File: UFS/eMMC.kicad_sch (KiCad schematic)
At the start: 7 parts, among them J13 513383474

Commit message: Relink hierarchical root: 18 sheets into RK3576 SBCv2 top level
Root was empty (no sheet boxes); all subsheets orphaned.
Rebuilt A1 top level linking RK3576, LPDDR5, Power, Ethernet,
HDMI, MIPI, PCIe, USB-A/C, Wireless, RTC, uSD, GPIO, OLED,
RP2350A, Connectors, Fixtures, DC_Power. block_diagrame kept
docs-only (unlinked, avoids double-instantiation). Lowercase
stub duplicates excluded. ERC: 1388 -> 770 violations.
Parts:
- renumbered C149 to C334, C147 to C335, C150 to C336, C148 to C337, C144 to C338, C143 to C339, J13 to J20
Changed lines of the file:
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@@
 		(polyline
 			(pts
-				(xy 57.785 33.02) (xy 43.815 33.02) (xy 43.815 50.165) (xy 57.785 50.165)
+				(xy 60.96 87.9475) (xy 60.96 65.405) (xy 40.64 65.4049) (xy 40.64 87.9474)
 			)
 			(stroke
 				(width 0)
 				(type dash)
-				(color 89 32 227 1)
+				(color 255 0 26 1)
 			)
 			(fill
@@
 		(polyline
 			(pts
-				(xy 60.96 64.77) (xy 42.545 64.77) (xy 42.545 88.9) (xy 60.96 88.9)
+				(xy 57.785 33.02) (xy 43.815 33.02) (xy 43.815 50.165) (xy 57.785 50.165)
 			)
 			(stroke
@@
 		(polyline
 			(pts
-				(xy 104.775 34.29) (xy 118.745 34.29) (xy 118.745 51.435) (xy 104.775 51.435)
+				(xy 61.595 64.77) (xy 42.545 64.77) (xy 42.545 88.9) (xy 61.595 88.9)
 			)
 			(stroke
@@
 			(fill
 				(type none)
+			)
+		)
+	)
+	(rule_area
+		(exclude_from_sim no)
+		(in_bom yes)
+		(on_board yes)
+		(dnp no)
+		(polyline
+			(pts
+				(xy 105.41 49.53) (xy 105.41 34.925) (xy 120.65 34.9249) (xy 120.65 49.5299)
+			)
+			(stroke
+				(width 0)
+				(type dash)
+				(color 255 0 26 1)
+			)
+			(fill
+				(type none)
+			)
+		)
+	)
+	(rule_area
+		(exclude_from_sim no)
+		(in_bom yes)
+		(on_board yes)
+		(dnp no)
+		(polyline
+			(pts
+				(xy 104.775 34.29) (xy 118.11 34.29) (xy 118.11 50.165) (xy 104.775 50.165)
+			)
+			(stroke
+				(width 0)
+				(type dash)
+				(color 89 32 227 1)
+			)
+			(fill
+				(type none)
+			)
+		)
+	)
+	(rule_area
+		(exclude_from_sim no)
+		(in_bom yes)
+		(on_board yes)
+		(dnp no)
+		(polyline
+			(pts
+				(xy 57.15 48.26) (xy 57.15 33.655) (xy 41.91 33.6549) (xy 41.91 48.2599)
+			)
+			(stroke
+				(width 0)
+				(type dash)
+				(color 255 0 26 1)
+			)
+			(fill
+				(type none)
+			)
+		)
+	)
+	(netclass_flag "Under PGA"
+		(length 1.27)
+		(shape round)
+		(at 120.65 35.56 270)
+		(effects
+			(font
+				(size 1.27 1.27)
+			)
+			(justify right bottom)
+		)
+		(property "Netclass" "100 OHM"
+			(at 125.476 35.56 0)
+			(show_name no)
+			(do_not_autoplace no)
+			(effects
+				(font
+					(size 0.762 0.762)
+					(color 255 0 26 1)
+				)
 			)
 		)
@@
 	)
 	(netclass_flag "Under PGA"
+		(length 1.27)
+		(shape round)
+		(at 41.91 34.29 90)
+		(effects
+			(font
+				(size 1.27 1.27)
+			)
+			(justify left bottom)
+		)
+		(property "Netclass" "100 OHM"
+			(at 37.084 34.29 0)
+			(show_name no)
+			(do_not_autoplace no)
+			(effects
+				(font
+					(size 0.762 0.762)
+					(color 255 0 26 1)
+				)
+			)
+		)
+	)
+	(netclass_flag "Under PGA"
 		(length 2.54)
 		(shape round)
@@
 				(font
 					(size 1.27 1.27)
+				)
+			)
+		)
+	)
+	(netclass_flag "Under PGA"
+		(length 1.27)
+		(shape round)
+		(at 40.64 66.04 90)
+		(effects
+			(font
+				(size 1.27 1.27)
+			)
+			(justify left bottom)
+		)
+		(property "Netclass" "50 OHM"
+			(at 36.068 66.04 0)
+			(show_name no)
+			(do_not_autoplace no)
+			(effects
+				(font
+					(size 0.762 0.762)
+					(color 255 0 26 1)
 				)
 			)
@@
 		(dnp no)
 		(fields_autoplaced yes)
-		(property "Reference" "J13"
+		(property "Reference" "J20"
 			(at 80.01 29.21 0)
 			(show_name no)
@@
 			(project "RK3576 SBCv2"
 				(path "/802f5b9f-44c6-4b1a-a63a-2c094d5816db/18e487aa-7d5d-4330-b69d-f75c2ebdb2cf"
-					(reference "J13")
+					(reference "J20")
 					(unit 1)
 				)
@@
 		(in_pos_files yes)
 		(dnp no)
-		(property "Reference" "#PWR0492"
+		(property "Reference" "#PWR0500"
 			(at 172.72 76.2 0)
 			(hide yes)
@@
 			(project "RK3576 SBCv2"
 				(path "/802f5b9f-44c6-4b1a-a63a-2c094d5816db/18e487aa-7d5d-4330-b69d-f75c2ebdb2cf"
-					(reference "#PWR0492")
+					(reference "#PWR0500")
 					(unit 1)
 				)
@@
 		(in_pos_files yes)
 		(dnp no)
-		(property "Reference" "#PWR0211"
+		(property "Reference" "#PWR0498"
 			(at 152.4 76.2 0)
 			(hide yes)
@@
 			(project "RK3576 SBCv2"
 				(path "/802f5b9f-44c6-4b1a-a63a-2c094d5816db/18e487aa-7d5d-4330-b69d-f75c2ebdb2cf"
-					(reference "#PWR0211")
+					(reference "#PWR0498")
 					(unit 1)
 				)
@@
 		(in_pos_files yes)
 		(dnp no)
-		(property "Reference" "#PWR0217"
+		(property "Reference" "#PWR0494"
 			(at 60.96 97.79 0)
 			(hide yes)
@@
 			(project "RK3576 SBCv2"
 				(path "/802f5b9f-44c6-4b1a-a63a-2c094d5816db/18e487aa-7d5d-4330-b69d-f75c2ebdb2cf"
-					(reference "#PWR0217")
+					(reference "#PWR0494")
 					(unit 1)
 				)
@@
 		(dnp no)
 		(fields_autoplaced yes)
-		(property "Reference" "C143"
+		(property "Reference" "C339"
 			(at 170.18 77.4762 0)
 			(show_name no)
@@
 			(project "RK3576 SBCv2"
 				(path "/802f5b9f-44c6-4b1a-a63a-2c094d5816db/18e487aa-7d5d-4330-b69d-f75c2ebdb2cf"
-					(reference "C143")
+					(reference "C339")
 					(unit 1)
 				)
@@
 		(in_pos_files yes)
 		(dnp no)
-		(property "Reference" "#PWR0210"
+		(property "Reference" "#PWR0496"
 			(at 134.62 76.2 0)
 			(hide yes)
@@
 			(project "RK3576 SBCv2"
 				(path "/802f5b9f-44c6-4b1a-a63a-2c094d5816db/18e487aa-7d5d-4330-b69d-f75c2ebdb2cf"
-					(reference "#PWR0210")
+					(reference "#PWR0496")
 					(unit 1)
 				)
@@
 		(dnp no)
 		(fields_autoplaced yes)
-		(property "Reference" "C149"
+		(property "Reference" "C334"
 			(at 121.92 82.5562 0)
 			(show_name no)
@@
 			(project "RK3576 SBCv2"
 				(path "/802f5b9f-44c6-4b1a-a63a-2c094d5816db/18e487aa-7d5d-4330-b69d-f75c2ebdb2cf"
-					(reference "C149")
+					(reference "C334")
 					(unit 1)
 				)
@@
 		(dnp no)
 		(fields_autoplaced yes)
-		(property "Reference" "J13"
+		(property "Reference" "J20"
 			(at 81.28 59.69 0)
 			(show_name no)
@@
 			(project "RK3576 SBCv2"
 				(path "/802f5b9f-44c6-4b1a-a63a-2c094d5816db/18e487aa-7d5d-4330-b69d-f75c2ebdb2cf"
-					(reference "J13")
+					(reference "J20")
 					(unit 2)
 				)
@@
 		(in_pos_files yes)
 		(dnp no)
-		(property "Reference" "#PWR0218"
+		(property "Reference" "#PWR0495"
 			(at 101.6 90.17 0)
 			(hide yes)
@@
 			(project "RK3576 SBCv2"
 				(path "/802f5b9f-44c6-4b1a-a63a-2c094d5816db/18e487aa-7d5d-4330-b69d-f75c2ebdb2cf"
-					(reference "#PWR0218")
+					(reference "#PWR0495")
 					(unit 1)
 				)
@@
 		(dnp no)
 		(fields_autoplaced yes)
-		(property "Reference" "C147"
+		(property "Reference" "C335"
 			(at 132.08 82.5562 0)
 			(show_name no)
@@
 			(project "RK3576 SBCv2"
 				(path "/802f5b9f-44c6-4b1a-a63a-2c094d5816db/18e487aa-7d5d-4330-b69d-f75c2ebdb2cf"
-					(reference "C147")
+					(reference "C335")
 					(unit 1)
 				)
@@
 		(dnp no)
 		(fields_autoplaced yes)
-		(property "Reference" "C150"
+		(property "Reference" "C336"
 			(at 140.97 80.0162 0)
 			(show_name no)
@@
 			(project "RK3576 SBCv2"
 				(path "/802f5b9f-44c6-4b1a-a63a-2c094d5816db/18e487aa-7d5d-4330-b69d-f75c2ebdb2cf"
-					(reference "C150")
+					(reference "C336")
 					(unit 1)
 				)
@@
 		(dnp no)
 		(fields_autoplaced yes)
-		(property "Reference" "C148"
+		(property "Reference" "C337"
 			(at 149.86 80.0162 0)
 			(show_name no)
@@
 			(project "RK3576 SBCv2"
 				(path "/802f5b9f-44c6-4b1a-a63a-2c094d5816db/18e487aa-7d5d-4330-b69d-f75c2ebdb2cf"
-					(reference "C148")
+					(reference "C337")
 					(unit 1)
 				)
@@
 		(in_pos_files yes)
 		(dnp no)
-		(property "Reference" "#PWR0213"
+		(property "Reference" "#PWR0497"
 			(at 134.62 92.71 0)
 			(hide yes)
@@
 			(project "RK3576 SBCv2"
 				(path "/802f5b9f-44c6-4b1a-a63a-2c094d5816db/18e487aa-7d5d-4330-b69d-f75c2ebdb2cf"
-					(reference "#PWR0213")
+					(reference "#PWR0497")
 					(unit 1)
 				)
@@
 		(in_pos_files yes)
 		(dnp no)
-		(property "Reference" "#PWR0216"
+		(property "Reference" "#PWR0493"
 			(at 60.96 54.61 0)
 			(hide yes)
@@
 			(project "RK3576 SBCv2"
 				(path "/802f5b9f-44c6-4b1a-a63a-2c094d5816db/18e487aa-7d5d-4330-b69d-f75c2ebdb2cf"
-					(reference "#PWR0216")
+					(reference "#PWR0493")
 					(unit 1)
 				)
@@
 		(in_pos_files yes)
 		(dnp no)
-		(property "Reference" "#PWR0206"
+		(property "Reference" "#PWR0501"
 			(at 172.72 87.63 0)
 			(hide yes)
@@
 			(project "RK3576 SBCv2"
 				(path "/802f5b9f-44c6-4b1a-a63a-2c094d5816db/18e487aa-7d5d-4330-b69d-f75c2ebdb2cf"
-					(reference "#PWR0206")
+					(reference "#PWR0501")
 					(unit 1)
 				)
@@
 		(dnp no)
 		(fields_autoplaced yes)
-		(property "Reference" "C144"
+		(property "Reference" "C338"
 			(at 160.02 77.4762 0)
 			(show_name no)
@@
 			(project "RK3576 SBCv2"
 				(path "/802f5b9f-44c6-4b1a-a63a-2c094d5816db/18e487aa-7d5d-4330-b69d-f75c2ebdb2cf"
-					(reference "C144")
+					(reference "C338")
 					(unit 1)
 				)
@@
 		(in_pos_files yes)
 		(dnp no)
-		(property "Reference" "#PWR0214"
+		(property "Reference" "#PWR0499"
 			(at 152.4 90.17 0)
 			(hide yes)
@@
 			(project "RK3576 SBCv2"
 				(path "/802f5b9f-44c6-4b1a-a63a-2c094d5816db/18e487aa-7d5d-4330-b69d-f75c2ebdb2cf"
-					(reference "#PWR0214")
+					(reference "#PWR0499")
 					(unit 1)
 				)

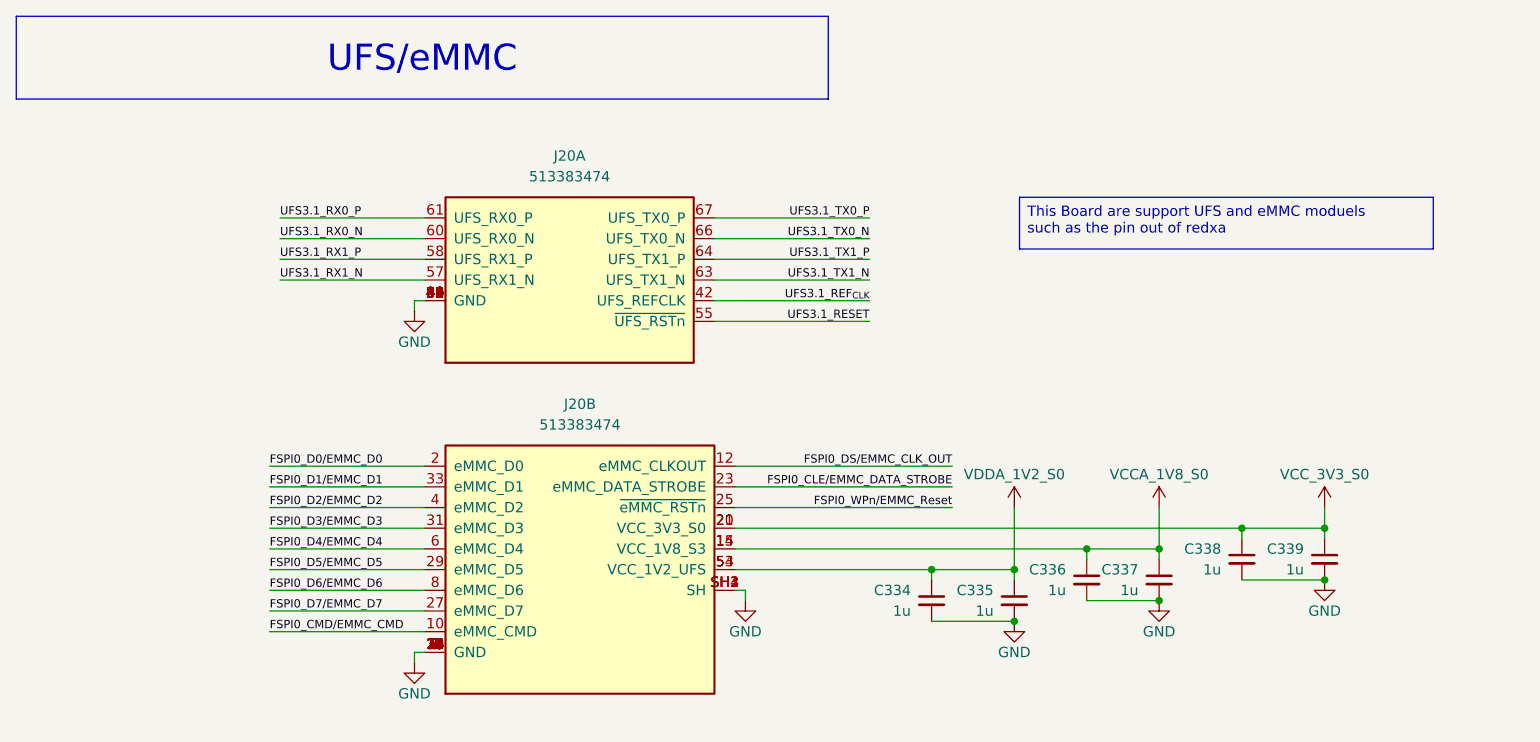
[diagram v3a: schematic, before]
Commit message: block diagrame with Hierarchical labels and NVMe SSD footprint
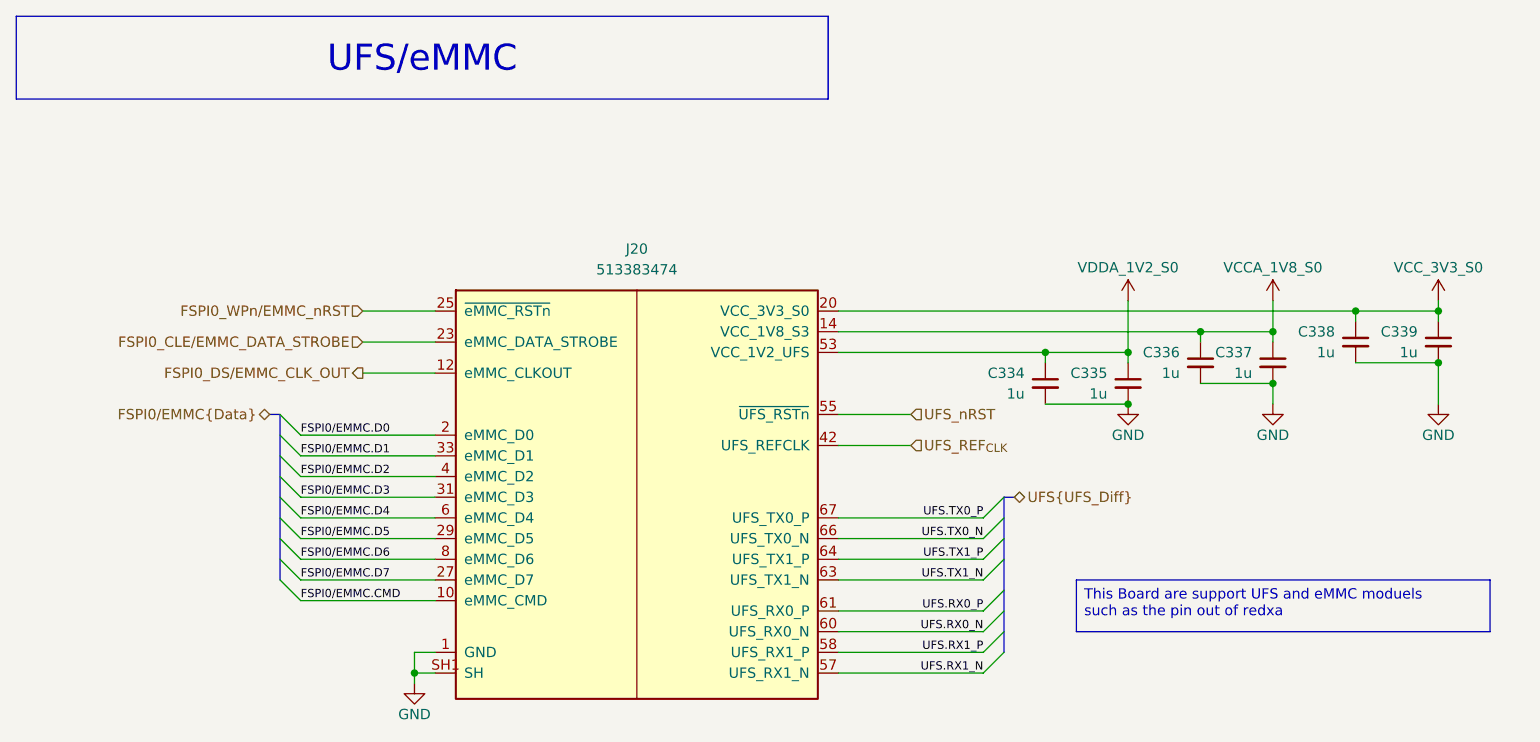
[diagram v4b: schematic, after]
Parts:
- removed unit 2 of J20
- J20: footprint Datasheet_Footprints:RADXA_UFS_MOD_30P34P -> Datasheet_Footprints:SBC_UFS_EMMC_2x513383474
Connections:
- net FSPI0_CLE/EMMC_DATA_STROBE: now also J20.23 (eMMC_DATA_STROBE)
- net FSPI0_DS/EMMC_CLK_OUT: now also J20.12 (eMMC_CLKOUT)
- net GND: now also J20.1 (GND), J20.11 (GND), J20.13 (GND), J20.16 (GND), J20.17 (GND), J20.18 (GND), J20.19 (GND), J20.22 (GND), J20.24 (GND), J20.26 (GND), J20.28 (GND), J20.3 (GND), J20.30 (GND), J20.32 (GND), J20.34 (GND), J20.5 (GND), J20.7 (GND), J20.9 (GND), J20.SH1 (SH), J20.SH2 (SH), J20.SH3 (SH), J20.SH4 (SH)
- net VCCA_1V8_S0: now also J20.14 (VCC_1V8_S3), J20.15 (VCC_1V8_S3)
- net VCC_3V3_S0: now also J20.20 (VCC_3V3_S0), J20.21 (VCC_3V3_S0)
- net UFS3.1_REF_{CLK} renamed UFS_REF_{CLK}
- net UFS3.1_RESET renamed UFS_nRST
- net UFS3.1_RX0_N renamed UFS.RX0_N
- net UFS3.1_RX0_P renamed UFS.RX0_P
- net UFS3.1_RX1_N renamed UFS.RX1_N
- net UFS3.1_RX1_P renamed UFS.RX1_P
- net UFS3.1_TX0_N renamed UFS.TX0_N
- net UFS3.1_TX0_P renamed UFS.TX0_P
- net UFS3.1_TX1_N renamed UFS.TX1_N
- net UFS3.1_TX1_P renamed UFS.TX1_P
- net VDDA_1V2_S0 renamed VCC_1V2_UFS
- net VCC_1V2_UFS: now also J20.53 (VCC_1V2_UFS), J20.54 (VCC_1V2_UFS)
- new net FSPI0_WPn/EMMC_nRST: J20.25 (~{eMMC_RSTn})
- new net FSPI0/EMMC.CMD: J20.10 (eMMC_CMD)
- new net FSPI0/EMMC.D0: J20.2 (eMMC_D0)
- new net FSPI0/EMMC.D1: J20.33 (eMMC_D1)
- new net FSPI0/EMMC.D2: J20.4 (eMMC_D2)
- new net FSPI0/EMMC.D3: J20.31 (eMMC_D3)
- new net FSPI0/EMMC.D4: J20.6 (eMMC_D4)
- new net FSPI0/EMMC.D5: J20.29 (eMMC_D5)
- new net FSPI0/EMMC.D6: J20.8 (eMMC_D6)
- new net FSPI0/EMMC.D7: J20.27 (eMMC_D7)
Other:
- moved on the sheet: C334, C335, C336, C337, C338, C339
